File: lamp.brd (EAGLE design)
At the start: 24.4 x 40.6 mm, 4 parts

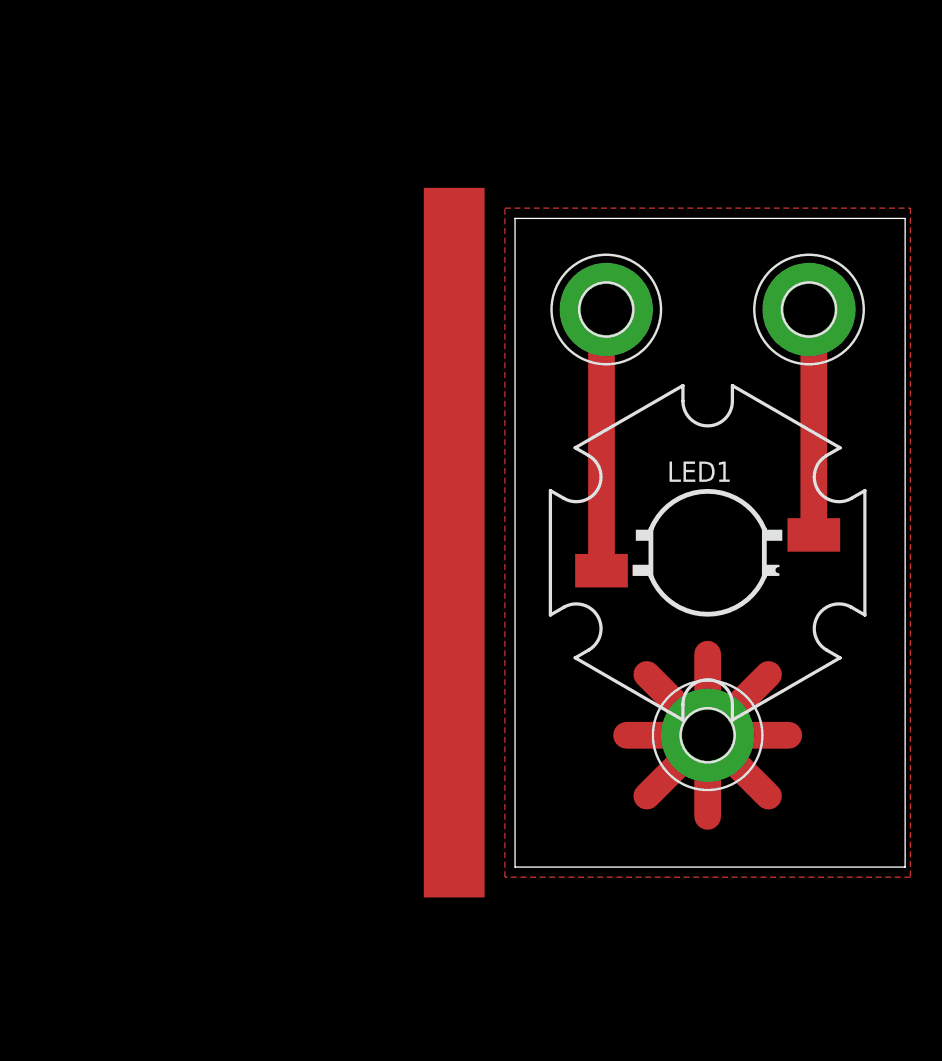
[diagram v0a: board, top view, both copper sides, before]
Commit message: Updated the PCB layout.
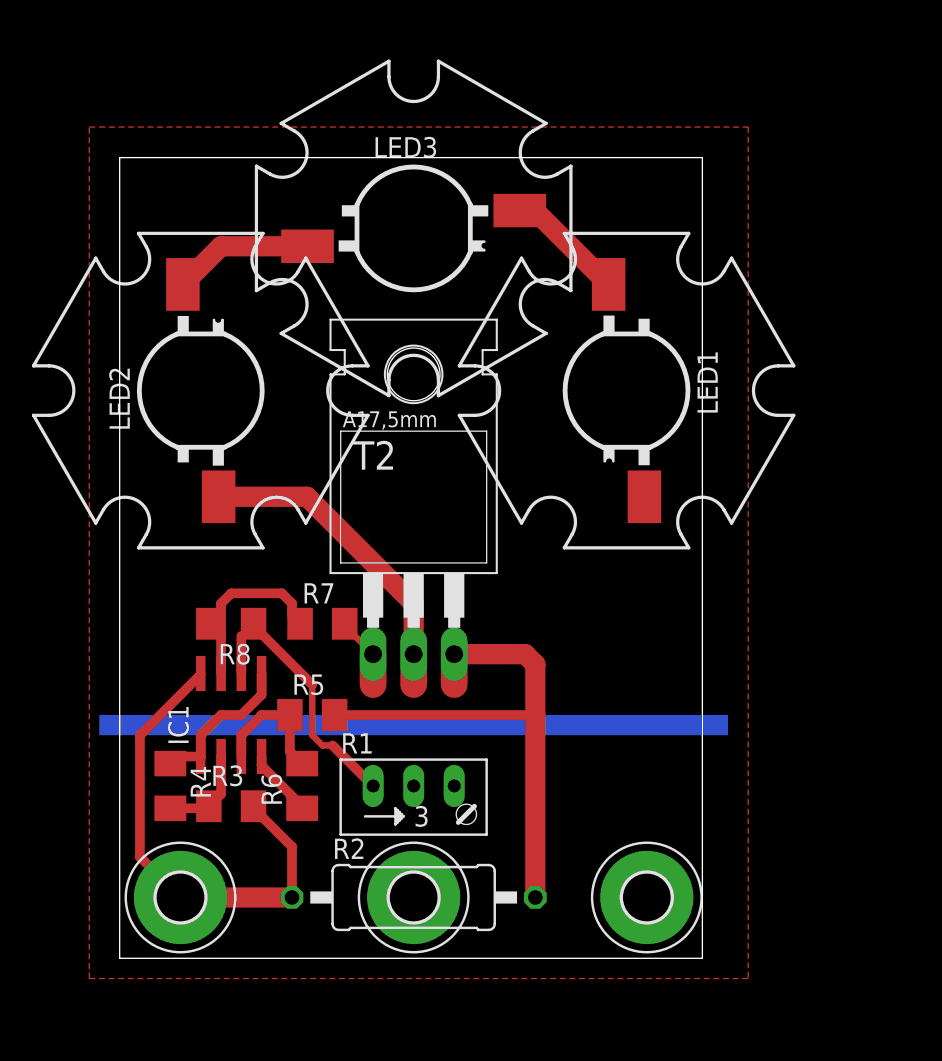
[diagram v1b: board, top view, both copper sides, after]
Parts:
- removed E$3: (no value), holes:3,2-PAD
- added IC1: LM358D, linear:SO08
- added LED2, LED3: Z-POWER-LED, led:Z-POWER-LED-PCB-TYPE
- added MOUNT: MOUNT-PAD-ROUND3.0, holes:3,0-PAD
- added R1: 10k, pot:RJ9W
- added R2: 0R1, resistor:0411/15
- added R3, R4, R5, R6: 470k, resistor:M1206
- added R7: 1k, resistor:M1206
- added R8: 47k, resistor:M1206
- added T2: TIP32C, transistor:TO220
- GND, VCC: value MOUNT-PAD-ROUND3.2 -> MOUNT-PAD-ROUND3.0; device holes:3,2-PAD -> holes:3,0-PAD
- moved VCC 45.5 mm to (3.81, 3.81)
- moved GND 38.2 mm to (33.0, 3.81)
- moved LED1 11.4 mm to (31.8, 35.6), turned to 270 degrees
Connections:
- removed net N$1: GND.B3,2, LED1.C
- new net GND: GND.B3,0, IC1.4, LED1.C, R1.S, R6.1
- new net N$10: IC1.6, R1.E, R8.1
- new net N$11: IC1.2, R3.1, R4.2
- new net N$12: IC1.3, R5.1, R6.2
- new net N$3: R7.2, T2.1
- new net N$4: IC1.7, R7.1, R8.2
- new net N$5: LED2.A, T2.2
- new net N$6: LED2.C, LED3.A
- new net N$7: LED1.A, LED3.C
- new net N$9: IC1.1, IC1.5, R4.1
- new net VCC: IC1.8, R2.1, R3.2, VCC.B3,0
- net N$2: now also R2.2, R5.2, T2.3; no longer LED1.A, VCC.B3,2
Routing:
- net HEAT: track 41.9 -> 0.00 mm
- net VCC: track 0.00 -> 30.4 mm
- net N$5: track 0.00 -> 20.1 mm
- net N$2: track 16.7 -> 34.4 mm
- net N$10: track 0.00 -> 17.1 mm
- net N$1: track 14.4 -> 0.00 mm
- net N$4: track 0.00 -> 11.9 mm
- net N$9: track 0.00 -> 9.61 mm
- net N$6: track 0.00 -> 8.79 mm
- net N$12: track 0.00 -> 8.26 mm
- net N$7: track 0.00 -> 7.48 mm
- net N$11: track 0.00 -> 5.90 mm
- net N$3: track 0.00 -> 4.55 mm
- net GND: track 0.00 -> 4.30 mm
- added copper zone on layer 1, net GND
- removed copper zone on layer 1, net HEAT
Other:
- board size 24.4 x 40.6 mm -> 36.5 x 50.2 mm

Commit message: Adjusted LED placement on the PCB.
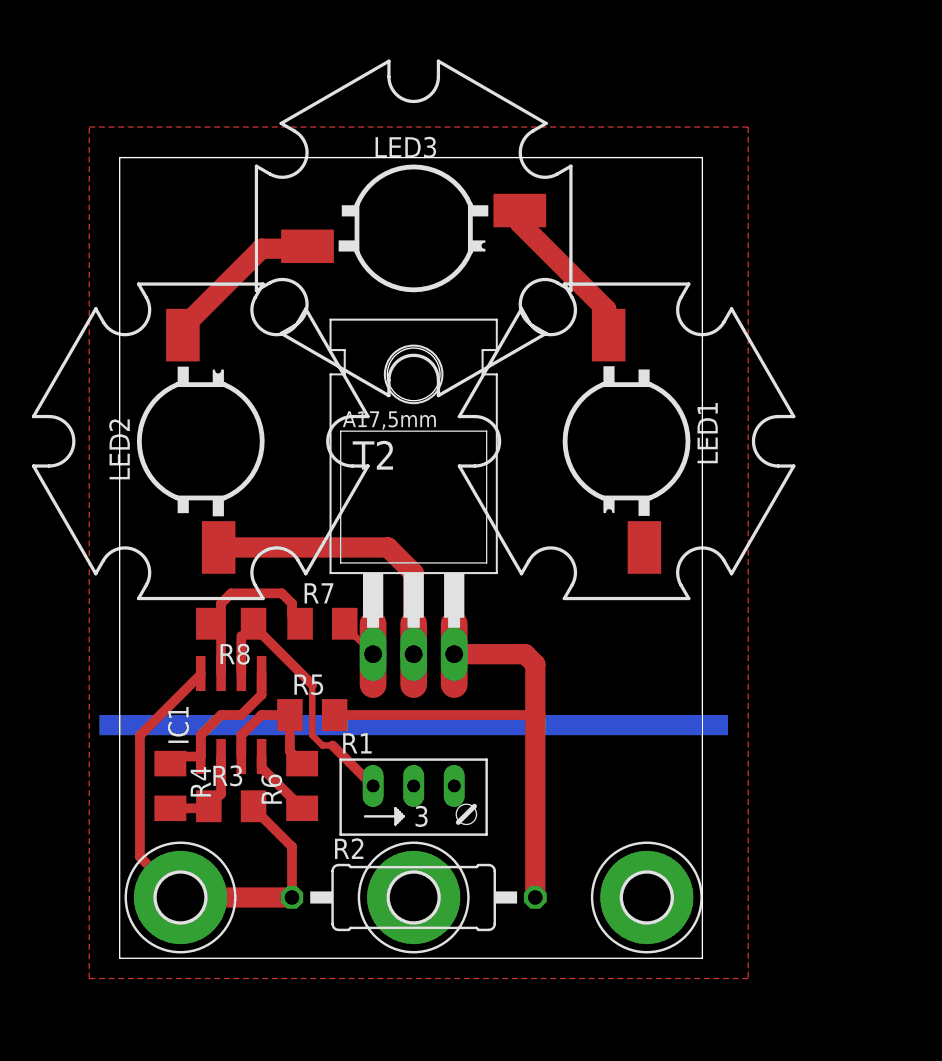
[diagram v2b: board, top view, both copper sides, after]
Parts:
- moved LED1 3.18 mm to (31.8, 32.4)
- moved LED2 3.18 mm to (5.08, 32.4)
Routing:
- net N$7: track 7.48 -> 10.1 mm
- net N$3: track 4.55 -> 6.45 mm
- net N$2: track 34.4 -> 36.3 mm
- net N$6: track 8.79 -> 10.4 mm
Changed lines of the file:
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@@
 <wire x1="0" y1="50.155" x2="0" y2="0" width="0" layer="20"/>
 <rectangle x1="-1.27" y1="13.97" x2="38.1" y2="15.24" layer="16"/>
-<circle x="5.08" y="35.56" radius="2.694075" width="0.6096" layer="41"/>
+<circle x="5.08" y="32.385" radius="2.694075" width="0.6096" layer="41"/>
 <circle x="18.415" y="45.72" radius="2.694075" width="0.6096" layer="41"/>
-<circle x="31.75" y="35.56" radius="2.694075" width="0.6096" layer="41"/>
+<circle x="31.75" y="32.385" radius="2.694075" width="0.6096" layer="41"/>
 </plain>
 <attributes>
@@
 </autorouter>
 <elements>
-<element name="LED1" library="led" package="Z-POWER-LED-PCB-TYPE" value="Z-POWER-LED" x="31.75" y="35.56" rot="R270"/>
+<element name="LED1" library="led" package="Z-POWER-LED-PCB-TYPE" value="Z-POWER-LED" x="31.75" y="32.385" rot="R270"/>
 <element name="IC1" library="linear" package="SO08" value="LM358D" x="6.985" y="15.24"/>
 <element name="R1" library="pot" package="RJ9W" value="10k" x="18.415" y="10.16"/>
@@
 <element name="R5" library="resistor" package="M1206" value="470k" x="12.065" y="15.24"/>
 <element name="R6" library="resistor" package="M1206" value="470k" x="11.43" y="10.795" rot="R90"/>
-<element name="LED2" library="led" package="Z-POWER-LED-PCB-TYPE" value="Z-POWER-LED" x="5.08" y="35.56" rot="R90"/>
+<element name="LED2" library="led" package="Z-POWER-LED-PCB-TYPE" value="Z-POWER-LED" x="5.08" y="32.385" rot="R90"/>
 <element name="LED3" library="led" package="Z-POWER-LED-PCB-TYPE" value="Z-POWER-LED" x="18.415" y="45.72"/>
 <element name="R7" library="resistor" package="M1206" value="1k" x="12.7" y="20.955"/>
@@
 <wire x1="13.465" y1="15.24" x2="26.035" y2="15.24" width="0.6096" layer="1"/>
 <wire x1="20.955" y1="19.05" x2="20.955" y2="17.145" width="1.6764" layer="1"/>
+<wire x1="20.955" y1="19.05" x2="20.955" y2="20.955" width="1.6764" layer="1"/>
 </signal>
 <signal name="N$3">
@@
 <wire x1="14.1" y1="20.825" x2="15.875" y2="19.05" width="0.4064" layer="1"/>
 <wire x1="15.875" y1="19.05" x2="15.875" y2="17.145" width="1.6764" layer="1"/>
+<wire x1="15.875" y1="19.05" x2="15.875" y2="20.955" width="1.6764" layer="1"/>
 </signal>
 <signal name="N$4">
@@
 <contactref element="T2" pad="2"/>
 <contactref element="LED2" pad="A"/>
-<wire x1="6.2" y1="28.91" x2="11.73" y2="28.91" width="1.27" layer="1"/>
-<wire x1="11.73" y1="28.91" x2="18.415" y2="22.225" width="1.27" layer="1"/>
-<wire x1="18.415" y1="19.05" x2="18.415" y2="22.225" width="1.27" layer="1"/>
 <wire x1="18.415" y1="19.05" x2="18.415" y2="17.145" width="1.6764" layer="1"/>
+<wire x1="6.2" y1="25.735" x2="16.81" y2="25.735" width="1.27" layer="1"/>
+<wire x1="16.81" y1="25.735" x2="18.415" y2="24.13" width="1.27" layer="1"/>
+<wire x1="18.415" y1="24.13" x2="18.415" y2="20.955" width="1.27" layer="1"/>
+<wire x1="18.415" y1="19.05" x2="18.415" y2="20.955" width="1.6764" layer="1"/>
 </signal>
 <signal name="N$6">
 <contactref element="LED2" pad="C"/>
 <contactref element="LED3" pad="A"/>
-<wire x1="11.765" y1="44.6" x2="6.35" y2="44.6" width="1.27" layer="1"/>
-<wire x1="6.35" y1="44.6" x2="3.96" y2="42.21" width="1.27" layer="1"/>
+<wire x1="3.96" y1="39.035" x2="3.96" y2="39.52" width="1.27" layer="1"/>
+<wire x1="3.96" y1="39.52" x2="8.89" y2="44.45" width="1.27" layer="1"/>
+<wire x1="8.89" y1="44.45" x2="11.615" y2="44.45" width="1.27" layer="1"/>
+<wire x1="11.615" y1="44.45" x2="11.765" y2="44.6" width="1.27" layer="1"/>
 </signal>
 <signal name="N$7">
 <contactref element="LED3" pad="C"/>
 <contactref element="LED1" pad="A"/>
-<wire x1="25.065" y1="46.84" x2="26" y2="46.84" width="1.27" layer="1"/>
-<wire x1="26" y1="46.84" x2="30.63" y2="42.21" width="1.27" layer="1"/>
+<wire x1="25.065" y1="46.84" x2="25.065" y2="46.055" width="1.27" layer="1"/>
+<wire x1="25.065" y1="46.055" x2="30.48" y2="40.64" width="1.27" layer="1"/>
+<wire x1="30.48" y1="40.64" x2="30.48" y2="39.185" width="1.27" layer="1"/>
+<wire x1="30.48" y1="39.185" x2="30.63" y2="39.035" width="1.27" layer="1"/>
 </signal>
 <signal name="GND">
@@
 <contactref element="IC1" pad="4"/>
 <polygon width="0.6096" layer="1" isolate="0.4064">
-<vertex x="-1.27" y="52.07"/>
+<vertex x="-1.905" y="52.07"/>
 <vertex x="39.37" y="52.07"/>
 <vertex x="39.37" y="-1.27"/>
 <vertex x="-1.905" y="-1.27"/>
-<vertex x="-1.905" y="52.07"/>
 </polygon>
-<wire x1="8.89" y1="12.64" x2="8.89" y2="12.065" width="0.6096" layer="1"/>
+<wire x1="8.89" y1="12.64" x2="8.89" y2="11.935" width="0.6096" layer="1"/>
 <wire x1="11.43" y1="9.395" x2="11.43" y2="9.525" width="0.6096" layer="1"/>
-<wire x1="11.43" y1="9.525" x2="8.89" y2="12.065" width="0.6096" layer="1"/>
+<wire x1="8.89" y1="11.935" x2="11.43" y2="9.395" width="0.6096" layer="1"/>
 </signal>
 <signal name="N$9">

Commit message: Whoops...
Swapped pins in the schematic, so gotta redo the entire PCB layout.
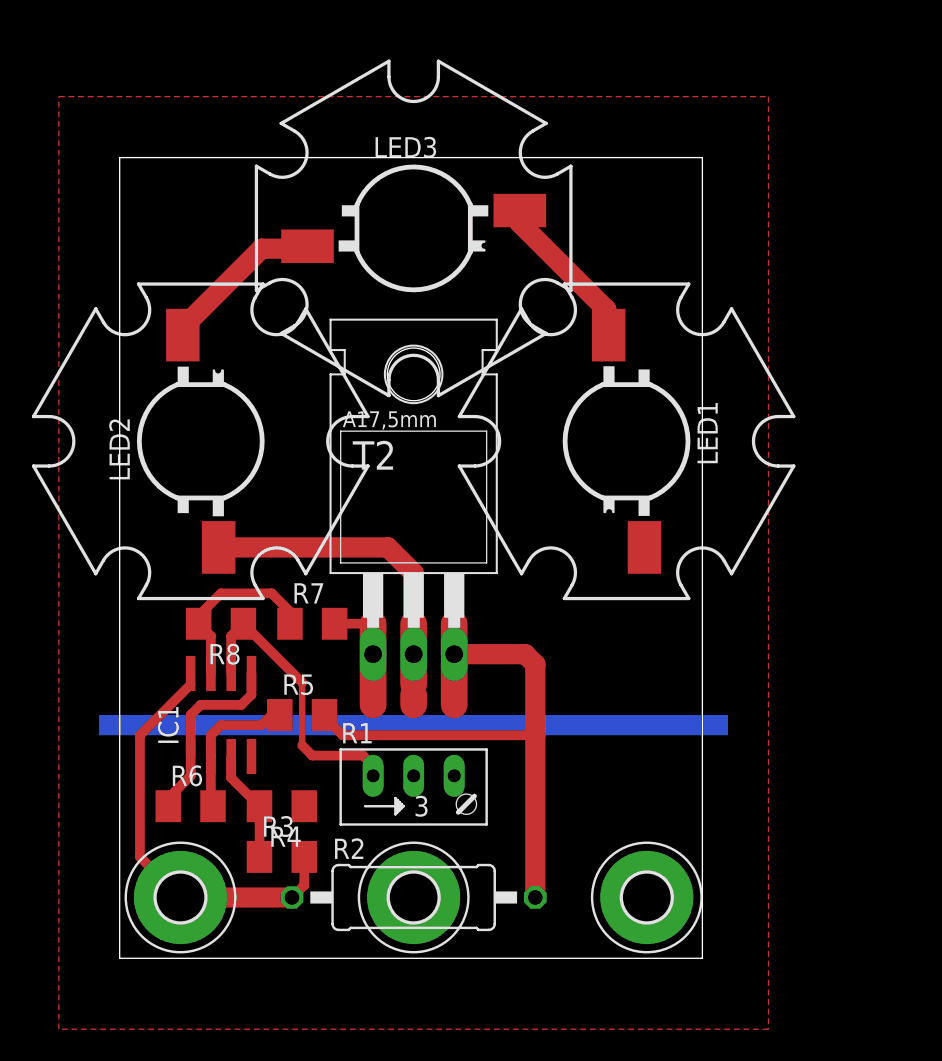
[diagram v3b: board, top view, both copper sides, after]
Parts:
- moved R4 7.10 mm to (10.2, 9.53), turned to 180 degrees
- moved R6 7.10 mm to (4.45, 9.53), turned to 0 degrees
- moved R3 4.49 mm to (10.2, 6.35)
- moved IC1 0.64 mm to (6.35, 15.2)
- moved R8 0.64 mm to (6.35, 21.0)
- moved R1 0.63 mm to (18.4, 10.8)
- moved R5 0.63 mm to (11.4, 15.2)
- moved R7 0.63 mm to (12.1, 21.0)
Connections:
- net GND: now also R4.1; no longer R6.1
- net N$11: now also IC1.3; no longer IC1.2
- net N$12: now also IC1.2; no longer IC1.3
- net N$9: now also R6.1; no longer R4.1
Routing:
- net GND: track 4.43 -> 0.00 mm
- net VCC: track 30.4 -> 26.2 mm
- net N$1: track 0.00 -> 2.54 mm
- net N$9: track 9.61 -> 12.0 mm
- net N$11: track 5.90 -> 7.03 mm
- net N$10: track 17.1 -> 18.2 mm
- net N$12: track 8.26 -> 9.34 mm
- net N$3: track 6.45 -> 7.49 mm
- net N$2: track 36.3 -> 35.7 mm
- net N$8: track 0.00 -> 0.64 mm

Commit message: Improved the design.
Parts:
- removed MOUNT: MOUNT-PAD-ROUND3.0, holes:3,0-PAD
- R2: device resistor:0411/15 -> resistor:0617/17
- moved T2 0.65 mm to (18.9, 25.9)
- moved R1 0.65 mm to (18.9, 11.3)
- moved R7 0.65 mm to (12.5, 21.4)
- moved R8 0.65 mm to (6.81, 21.4)
- moved LED3 0.65 mm to (18.9, 46.2)
- moved IC1 0.65 mm to (6.81, 15.7)
- moved R3 0.65 mm to (10.6, 6.81)
- moved R4 0.65 mm to (10.6, 9.99)
- moved R5 0.65 mm to (11.9, 15.7)
- moved R6 0.65 mm to (4.90, 9.99)
- moved VCC 0.65 mm to (4.27, 4.27)
- moved LED2 0.65 mm to (5.54, 32.8)
- moved GND 0.65 mm to (33.5, 4.27)
- moved LED1 0.65 mm to (32.2, 32.8)
- moved R2 0.43 mm to (18.7, 4.15), flipped to the bottom, turned to 180 degrees
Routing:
- net GND: track 0.00 -> 10.9 mm
- net N$20: track 0.00 -> 2.82 mm
- net N$19: track 0.00 -> 2.76 mm
- net N$13: track 0.00 -> 2.12 mm
- net N$15: track 0.00 -> 1.60 mm
- net N$18: track 0.00 -> 1.03 mm
- net VCC: track 26.2 -> 25.6 mm
- net N$10: track 18.2 -> 17.6 mm
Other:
- board size 36.5 x 50.2 mm -> 37.4 x 50.6 mm

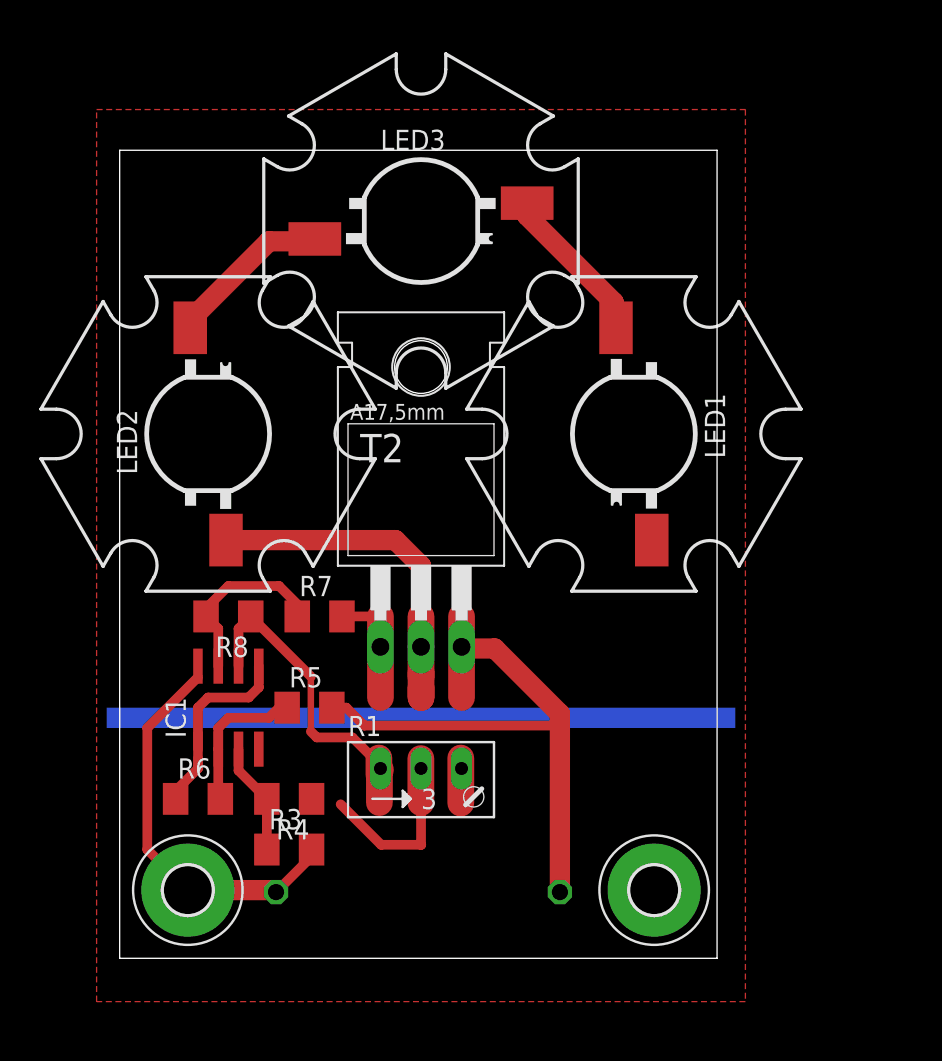
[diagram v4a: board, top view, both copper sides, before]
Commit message: Redesigned the PCB to accomodate the SMD shunt.
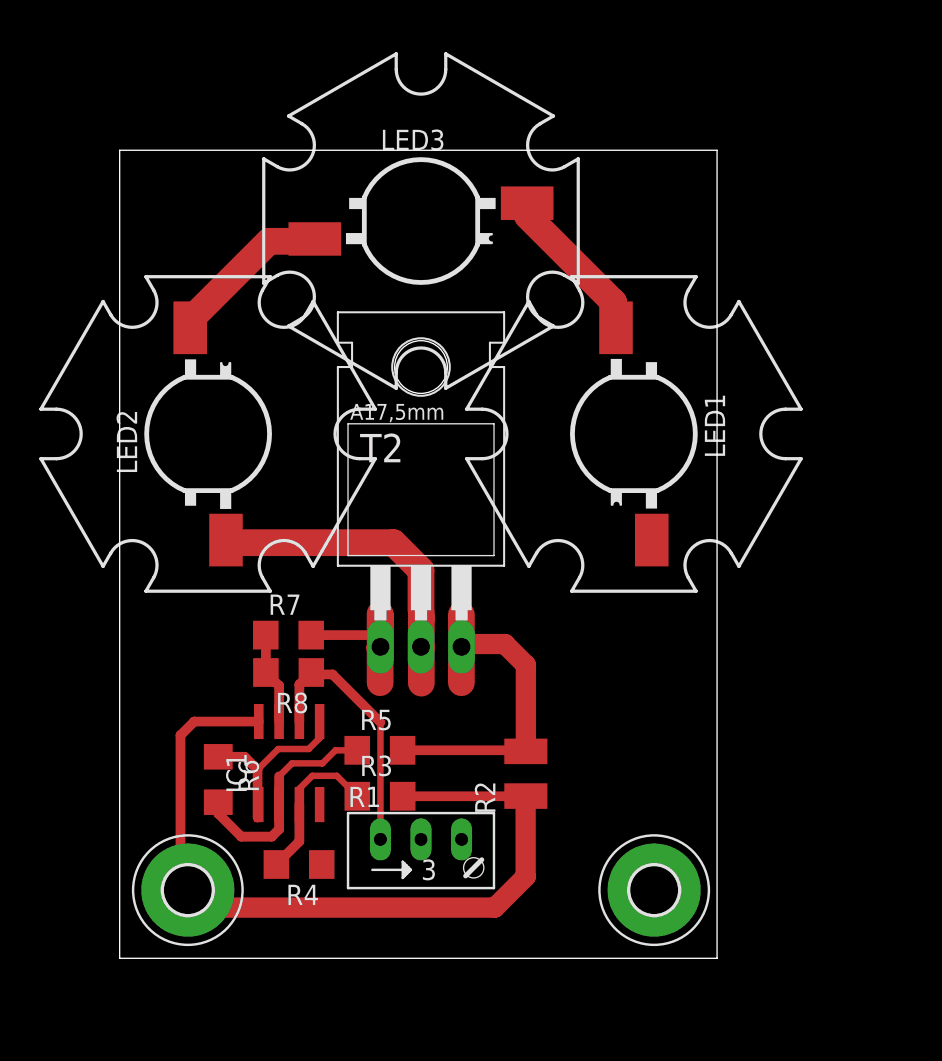
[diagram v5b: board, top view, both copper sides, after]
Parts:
- R2: value 0R1 -> 1R0; device resistor:0617/17 -> resistor:R1210
- R3, R4, R5, R6, R7, R8: device resistor:M1206 -> resistor:R1206
- moved R2 10.0 mm to (25.4, 11.6), flipped to the top, turned to 90 degrees
- moved R3 6.59 mm to (16.3, 10.1)
- moved R5 5.16 mm to (16.3, 13.0)
- moved R8 5.16 mm to (10.6, 17.9)
- moved IC1 5.15 mm to (10.6, 12.2)
- moved R1 4.45 mm to (18.9, 6.81)
- moved R4 4.16 mm to (11.2, 5.88)
- moved R7 2.27 mm to (10.6, 20.2)
- moved R6 1.76 mm to (6.18, 11.2), turned to 270 degrees
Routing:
- net VCC: track 25.6 -> 53.5 mm
- net N$2: track 35.7 -> 17.8 mm
- net GND: track 10.9 -> 0.00 mm
- net N$4: track 11.6 -> 5.76 mm
- net N$12: track 9.34 -> 14.2 mm
- net N$22: track 0.00 -> 4.35 mm
- net N$17: track 0.00 -> 4.32 mm
- net N$23: track 0.00 -> 4.27 mm
- net N$3: track 7.49 -> 4.64 mm
- net N$20: track 2.82 -> 0.00 mm
- net N$11: track 7.03 -> 9.84 mm
- net N$19: track 2.76 -> 0.00 mm
- net N$1: track 2.54 -> 0.00 mm
- net N$13: track 2.12 -> 0.00 mm
- net N$5: track 19.9 -> 17.8 mm
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- removed copper zone on layer 1, net GND
